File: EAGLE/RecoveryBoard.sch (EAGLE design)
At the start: 74 parts, among them IC1 BD62120AEFJ-E2, Q6 MOSFET-PCH-SOT23-6, U1 STM32F042K6, U10 TPS63070, Y1 ECS-160-10-36Q-ES-TR

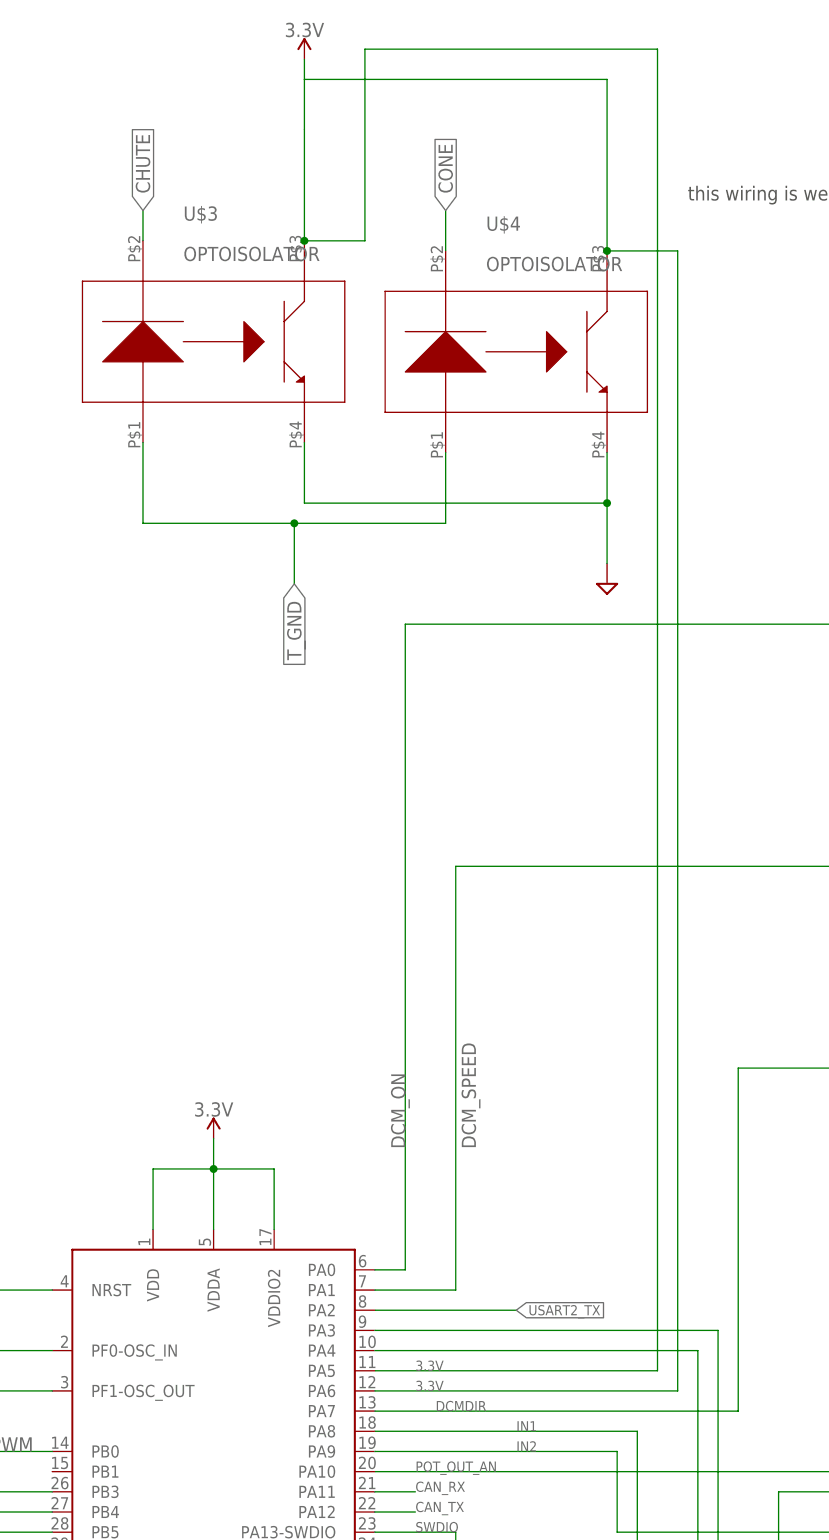
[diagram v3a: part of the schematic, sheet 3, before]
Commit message: updating STM32F0 pins
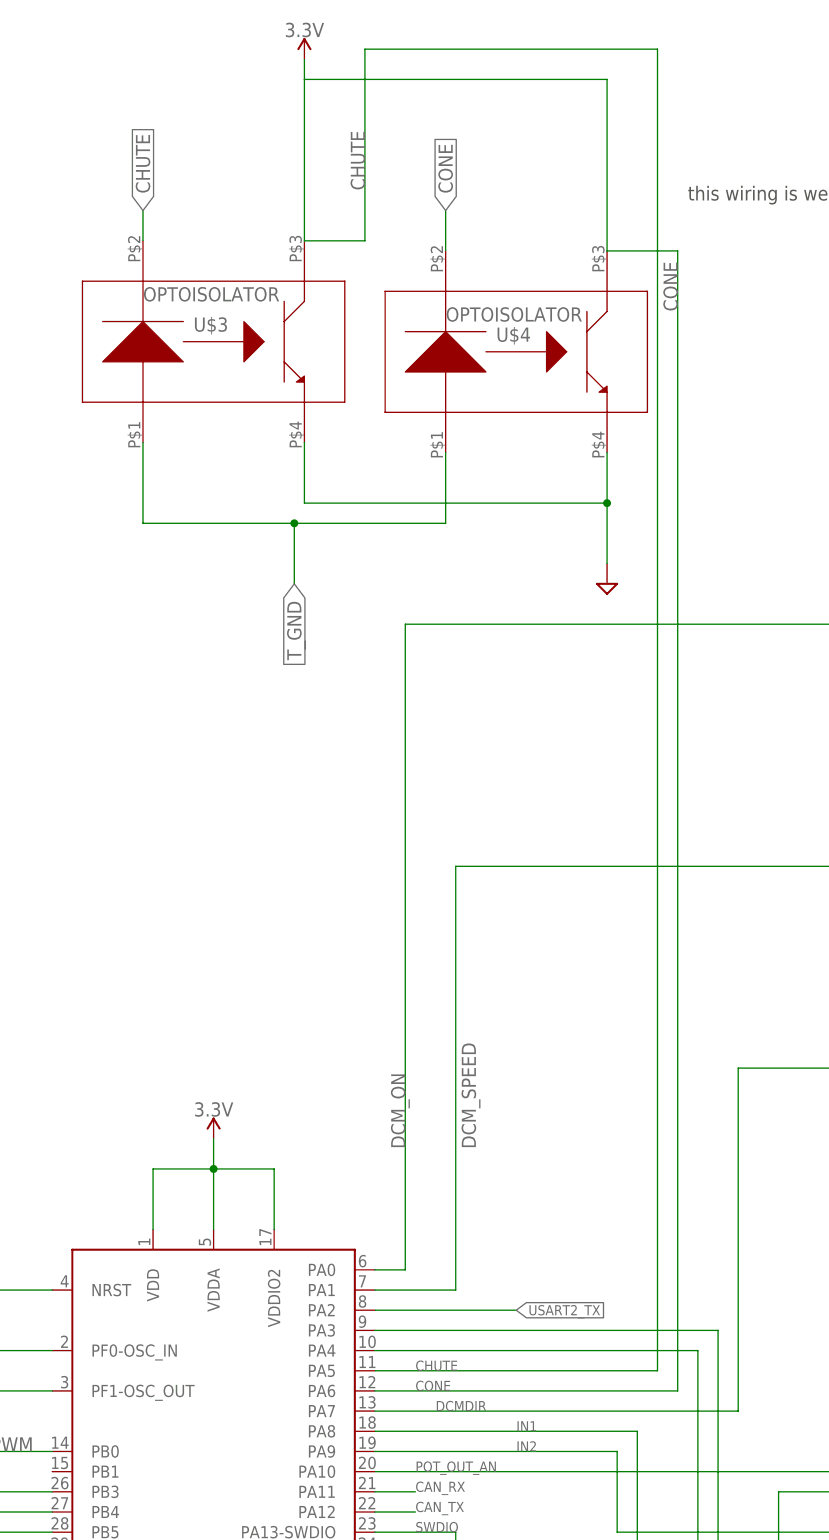
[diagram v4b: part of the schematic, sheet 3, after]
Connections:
- net 3.3V: no longer U1.PA5, U1.PA6
- net CHUTE: now also U1.PA5
- net CONE: now also U1.PA6
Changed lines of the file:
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@@
 <instance part="SUPPLY44" gate="GND" x="71.12" y="162.56" smashed="yes"/>
 <instance part="U$3" gate="G$1" x="275.59" y="322.58" smashed="yes">
-<attribute name="NAME" x="270.51" y="337.82" size="1.778" layer="95"/>
-<attribute name="VALUE" x="270.51" y="332.74" size="1.778" layer="96"/>
+<attribute name="NAME" x="271.78" y="323.85" size="1.778" layer="95"/>
+<attribute name="VALUE" x="265.43" y="327.66" size="1.778" layer="96"/>
 </instance>
 <instance part="U$4" gate="G$1" x="313.69" y="321.31" smashed="yes">
-<attribute name="NAME" x="308.61" y="336.55" size="1.778" layer="95"/>
-<attribute name="VALUE" x="308.61" y="331.47" size="1.778" layer="96"/>
+<attribute name="NAME" x="309.88" y="322.58" size="1.778" layer="95"/>
+<attribute name="VALUE" x="303.53" y="325.12" size="1.778" layer="96"/>
 </instance>
 <instance part="SUPPLY7" gate="G$1" x="285.75" y="358.14" smashed="yes">
@@
 </segment>
 <segment>
-<pinref part="SUPPLY7" gate="G$1" pin="3.3V"/>
 <pinref part="U$3" gate="G$1" pin="COLL"/>
-<wire x1="285.75" y1="358.14" x2="285.75" y2="355.6" width="0.1524" layer="91"/>
-<wire x1="285.75" y1="349.25" x2="285.75" y2="335.28" width="0.1524" layer="91"/>
-<wire x1="285.75" y1="335.28" x2="293.37" y2="335.28" width="0.1524" layer="91"/>
-<wire x1="293.37" y1="335.28" x2="293.37" y2="359.41" width="0.1524" layer="91"/>
-<junction x="285.75" y="335.28"/>
-<pinref part="U1" gate="G$1" pin="PA5"/>
-<label x="299.72" y="193.04" size="1.27" layer="95"/>
-<wire x1="294.64" y1="193.04" x2="330.2" y2="193.04" width="0.1524" layer="91"/>
-<wire x1="293.37" y1="359.41" x2="330.2" y2="359.41" width="0.1524" layer="91"/>
-<wire x1="330.2" y1="359.41" x2="330.2" y2="193.04" width="0.1524" layer="91"/>
 <pinref part="U$4" gate="G$1" pin="COLL"/>
 <wire x1="323.85" y1="355.6" x2="323.85" y2="334.01" width="0.1524" layer="91"/>
-<junction x="323.85" y="334.01"/>
-<wire x1="332.74" y1="334.01" x2="323.85" y2="334.01" width="0.1524" layer="91"/>
-<pinref part="U1" gate="G$1" pin="PA6"/>
-<wire x1="332.74" y1="190.5" x2="294.64" y2="190.5" width="0.1524" layer="91"/>
-<wire x1="332.74" y1="190.5" x2="332.74" y2="334.01" width="0.1524" layer="91"/>
-<label x="299.72" y="190.5" size="1.27" layer="95"/>
-<wire x1="285.75" y1="349.25" x2="285.75" y2="355.6" width="0.1524" layer="91"/>
+<pinref part="SUPPLY7" gate="G$1" pin="3.3V"/>
+<wire x1="285.75" y1="358.14" x2="285.75" y2="355.6" width="0.1524" layer="91"/>
 <wire x1="285.75" y1="355.6" x2="323.85" y2="355.6" width="0.1524" layer="91"/>
+<wire x1="285.75" y1="355.6" x2="285.75" y2="335.28" width="0.1524" layer="91"/>
 </segment>
 </net>
@@
 <label x="265.43" y="339.09" size="1.778" layer="95" rot="R90" xref="yes"/>
 </segment>
+<segment>
+<pinref part="U1" gate="G$1" pin="PA5"/>
+<wire x1="294.64" y1="193.04" x2="330.2" y2="193.04" width="0.1524" layer="91"/>
+<wire x1="293.37" y1="335.28" x2="293.37" y2="359.41" width="0.1524" layer="91"/>
+<wire x1="293.37" y1="359.41" x2="330.2" y2="359.41" width="0.1524" layer="91"/>
+<wire x1="330.2" y1="359.41" x2="330.2" y2="193.04" width="0.1524" layer="91"/>
+<label x="299.72" y="193.04" size="1.27" layer="95"/>
+<wire x1="293.37" y1="335.28" x2="285.75" y2="335.28" width="0.1524" layer="91"/>
+<label x="293.37" y="341.63" size="1.778" layer="95" rot="R90"/>
+</segment>
 </net>
 <net name="CONE" class="0">
@@
 <label x="303.53" y="339.09" size="1.778" layer="95" rot="R90" xref="yes"/>
 </segment>
-</net>
+<segment>
+<pinref part="U1" gate="G$1" pin="PA6"/>
+<wire x1="332.74" y1="190.5" x2="294.64" y2="190.5" width="0.1524" layer="91"/>
+<wire x1="332.74" y1="190.5" x2="332.74" y2="334.01" width="0.1524" layer="91"/>
+<label x="299.72" y="190.5" size="1.27" layer="95"/>
+<wire x1="332.74" y1="334.01" x2="323.85" y2="334.01" width="0.1524" layer="91"/>
+<label x="332.74" y="326.39" size="1.778" layer="95" rot="R90"/>
+</segment>
+</net>

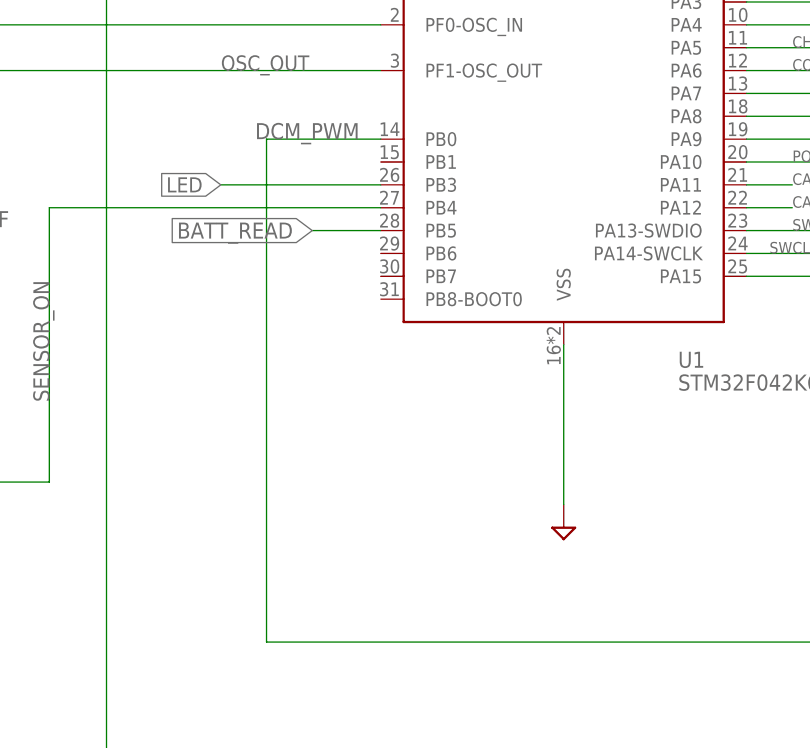
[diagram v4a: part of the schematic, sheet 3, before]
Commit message: added buzzer
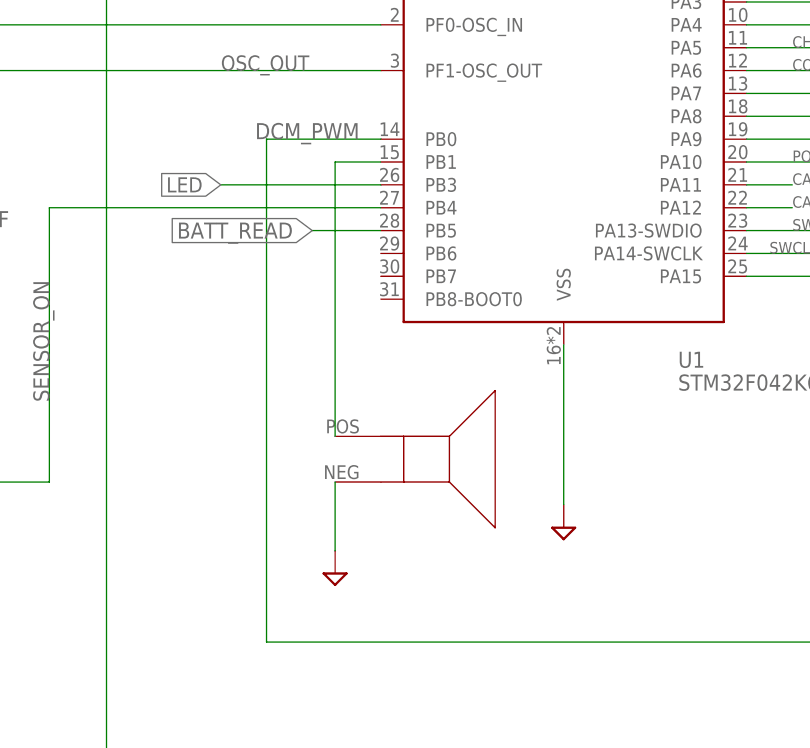
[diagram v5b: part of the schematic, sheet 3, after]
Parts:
- added U$7: SMT-0440-S-R, SPK--SMT-0440-S-R--Speaker:SMT-0440-S-R
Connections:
- new net N$24: U$7.POS, U1.PB1
- net GND: now also U$7.NEG
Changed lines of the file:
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@@
 <part name="C17" library="rcl" library_urn="urn:adsk.eagle:library:334" deviceset="C-US" device="C0402" package3d_urn="urn:adsk.eagle:package:23626/2" value="0.1uF"/>
 <part name="SUPPLY18" library="supply2" library_urn="urn:adsk.eagle:library:372" deviceset="GND" device=""/>
+<part name="U$7" library="SPK--SMT-0440-S-R--Speaker" deviceset="SMT-0440-S-R" device=""/>
+<part name="SUPPLY19" library="supply2" library_urn="urn:adsk.eagle:library:372" deviceset="GND" device=""/>
 </parts>
 <sheets>
@@
 <attribute name="VALUE" x="464.058" y="270.51" size="1.778" layer="96" rot="R270"/>
 </instance>
+<instance part="U$7" gate="G$1" x="261.62" y="147.32" smashed="yes"/>
+<instance part="SUPPLY19" gate="GND" x="248.92" y="134.62" smashed="yes"/>
 </instances>
 <busses>
@@
 <pinref part="R14" gate="G$1" pin="2"/>
 <pinref part="SUPPLY39" gate="GND" pin="GND"/>
+</segment>
+<segment>
+<pinref part="U$7" gate="G$1" pin="NEG"/>
+<wire x1="248.92" y1="144.78" x2="248.92" y2="137.16" width="0.1524" layer="91"/>
+<pinref part="SUPPLY19" gate="GND" pin="GND"/>
 </segment>
 </net>
@@
 </segment>
 </net>
+<net name="N$24" class="0">
+<segment>
+<pinref part="U1" gate="G$1" pin="PB1"/>
+<wire x1="254" y1="180.34" x2="248.92" y2="180.34" width="0.1524" layer="91"/>
+<wire x1="248.92" y1="180.34" x2="248.92" y2="149.86" width="0.1524" layer="91"/>
+<pinref part="U$7" gate="G$1" pin="POS"/>
+</segment>
+</net>

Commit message: Fixed some power issues with Ben.
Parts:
- removed BATTERY: (no value), pinhead:PINHD-1X5
- added JP1: (no value), pinhead:PINHD-1X4
- C11: device rcl:C-USC0402 -> oresat-rcl:C-EU0805-C-NOSILK
- C12, C13, C14, C16, C17: device rcl:C-USC0402 -> oresat-rcl:C-EU0603-C-NOSILK
- R15, R16: device rcl_custom:R-US_0402-B-NOSILK -> oresat-rcl:R-US_0603-C-NOSILK
- R17, R18, R19, R20, R21: device rcl:R-US_R0402 -> oresat-rcl:R-US_0603-C-NOSILK
- R22: device rcl:R-US_R0402 -> oresat-rcl:R-US_1206-C
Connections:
- net +18V renamed VUMB
- removed net BATT_CHARGE: BATTERY.5, C17.1, R22.1, U$5.BATT
- net +12V: now also C17.1, JP1.1, JP1.2, R22.1, U$5.BATT; no longer BATTERY.1
- net GND: now also JP1.3, JP1.4; no longer BATTERY.2
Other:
- note removed: "will the charger power the entire board like this?"

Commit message: Microcontroller and sensor board cleanup; added more to the outside world.
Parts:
- removed D3: X-QE, D-Cree-XQE-LED:X-QE
- removed OUTSIDE_WORLD: (no value), pinhead:PINHD-1X5
- added C18, C19, C20: 100n, rcl:C-EUC0402
- added JP2: (no value), pinhead:PINHD-1X7
- added R23, R25: 1k, oresat-rcl:R-US_0603-C-NOSILK
- added R24: 10k, oresat-rcl:R-US_0603-C-NOSILK
- added R26, R27: TBD, rcl:R-US_R0402
- added R28, R29: 10k, rcl:R-US_R0402
- R19: value (none) -> 10k
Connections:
- removed net CONE: OUTSIDE_WORLD.4, U$4.CATH, U1.PA6
- new net ACOK: R19.1, U$5.~ACOK
- new net DROGUE: JP2.4, U$4.CATH
- new net ISO-CHUTE: R28.1, U$3.EMIT, U1.PA5
- new net ISO-DROGUE: R29.1, U$4.EMIT, U1.PA6
- new net N$25: C17.1, JP1.1, JP1.2, R15.2, R22.1, R25.2, U$5.BATT
- new net N$26: R27.1, U$4.ANOD
- new net N$27: R8.2, R9.2, U$2.D
- new net VBAT: JP2.7, R25.1
- net +12V: no longer C17.1, JP1.1, JP1.2, R15.2, R22.1, U$5.BATT
- net 3.3V: now also C18.1, C19.1, C20.1, R19.2, SENSOR.ANOD, SENSOR.COLL, SENSOR2.ANOD, SENSOR2.COLL; no longer U$2.D
- net CHUTE: now also JP2.3; no longer OUTSIDE_WORLD.3, U1.PA5
- net GND: now also C18.2, C19.2, C20.2, JP2.2, R24.1, R28.2, R29.2, U$2.S, U$5.~EN; no longer OUTSIDE_WORLD.2, R8.2, R9.2, U$3.EMIT, U$4.EMIT
- net N$14: no longer R19.2
- net N$15: now also JP2.6, R23.2; no longer D3.C, U$5.~ACOK
- net N$16: now also R23.1, R24.2; no longer D3.A, R19.1
- net N$7: now also R26.1, U$3.ANOD; no longer SENSOR.ANOD, SENSOR.COLL, SENSOR2.ANOD, SENSOR2.COLL, U$2.S
- net T_GND: now also JP2.5, R26.2, R27.2; no longer OUTSIDE_WORLD.5, U$3.ANOD, U$4.ANOD
- net VUMB: now also JP2.1; no longer OUTSIDE_WORLD.1
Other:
- note added: "19V umbilical"
- note added: "ARM 1"
- note added: "ARM 2"
- note added: "Drogue Deploy Motor"
- note added: "Main Deploy Linear Actuator"
- note added: "Opto-isolated Inputs From Telemetrum"
- note added: "PUT PCHANNEL HERE"
- note added: "SHORT TO DISARM"
- note added: "TO 3S1P battery"
- note added: "TODO: CHECK ON OPTO ISOLATOR LED POLARITY AND CHOOES OI"
- note removed: "for ~EN, says On/Off not sure what that means?"
- note removed: "this wiring is weird...can't name a net for chute and cone"
- moved on the sheet: C1, C2, DCMOTOR, IC1, LA, Q6, R10, R11, R12, R14, R19, R32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

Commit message: starting grouping board components for layout
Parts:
- added C21: 10uF, oresat-rcl:C-EU0805-C-NOSILK
- added D3: X-QE, D-Cree-XQE-LED:X-QE
- added R30: (no value), oresat-rcl:R-US_0603-C-NOSILK
- added U$8: AO6405, Q--AO6405--P-CH MOSFET for Arm Switch:AO6405
- C12: value 4.7uF -> 10uF; device oresat-rcl:C-EU0603-C-NOSILK -> oresat-rcl:C-EU0805-C-NOSILK
- C14: value 2.2nF -> 0.1uF
- C15: device rcl:C-USC0402 -> oresat-rcl:C-EU0603-C-NOSILK
- C17: value 0.1uF -> 22uF
- R15: value 150K -> 2636
- R16: value 150K -> 1000
- R20: value 2.5K -> (none)
- U$3, U$4: value OPTOISOLATOR -> H11L1S(TA); device OptoIsolator:OPTOISOLATOR -> Q--H11L1S(TA)--OptoIsolator:H11L1S(TA)
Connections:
- removed net N$19 (its old number): C14.1, R20.1
- new net N$12: C21.1, R17.2, R18.2, R30.2, U$5.CELLS, U$5.VREF33
- new net N$23: C17.1, JP1.1, JP1.2, R15.2, R22.1, R25.2, U$5.BATT, U$8.S
- new net N$29: R29.1, U$4.EMIT
- net +12V: now also U$8.D
- net ACOK: now also D3.C, U1.PB7
- net CHUTE: now also U$3.ANOD; no longer U$3.CATH
- net DROGUE: now also U$4.ANOD; no longer U$4.CATH
- net GND: now also C21.2
- net ISO-CHUTE: now also U$3.OUTPUT; no longer R28.1, U$3.EMIT
- net ISO-DROGUE: now also U$4.OUTPUT; no longer R29.1, U$4.EMIT
- net N$14: now also D3.A, R30.1; no longer R17.2, R18.2, U$5.CELLS, U$5.VREF33
- net N$16: now also U$8.G
- net N$25: now also R28.1, U$3.EMIT; no longer C17.1, JP1.1, JP1.2, R15.2, R22.1, R25.2, U$5.BATT
- net N$26: now also U$4.CAT; no longer U$4.ANOD
- net N$7: now also U$3.CAT; no longer U$3.ANOD
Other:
- note added: "Do we still need an Arm input? there is no state where the board has power and is disarmed...this would free up a pin for a lock button"
- note removed: "PUT PCHANNEL HERE"
- note removed: "TODO: CHECK ON OPTO ISOLATOR LED POLARITY AND CHOOES OI"
- note removed: "what input voltage to calcualte ratio with? 12?"
- moved on the sheet: C11, C12, C13, C14, C16, C17, D1, D2, D4, JP1, JP2, L2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
